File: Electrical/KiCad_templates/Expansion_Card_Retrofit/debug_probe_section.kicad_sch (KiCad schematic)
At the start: 15 parts, among them U3 W25Q16JVUXIQ, U4 RP2040

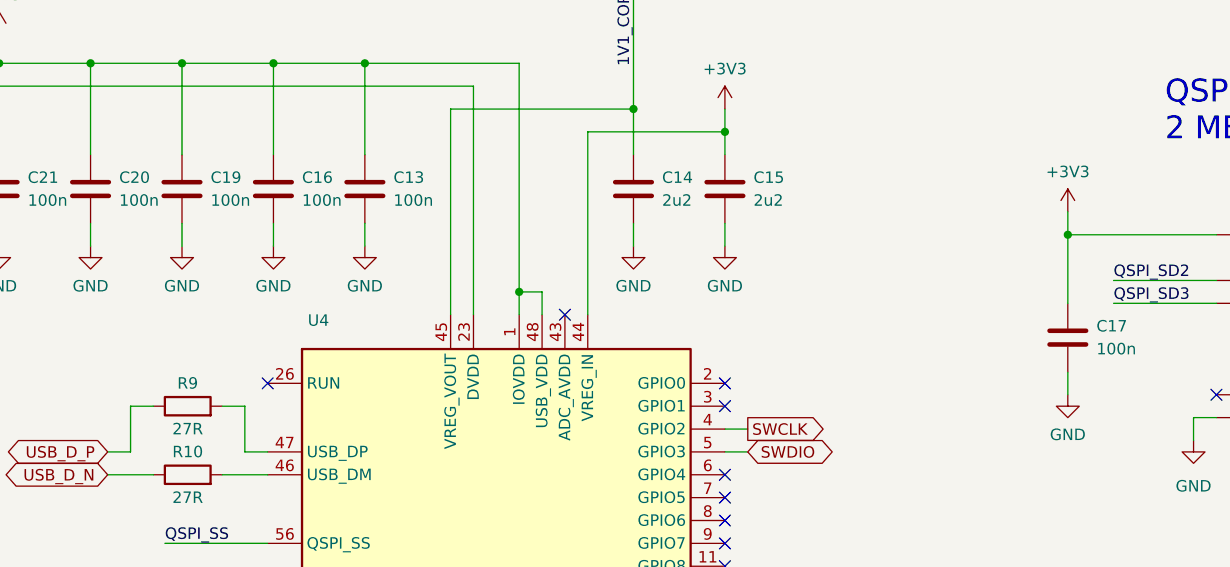
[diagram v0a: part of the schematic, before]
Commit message: Added test points
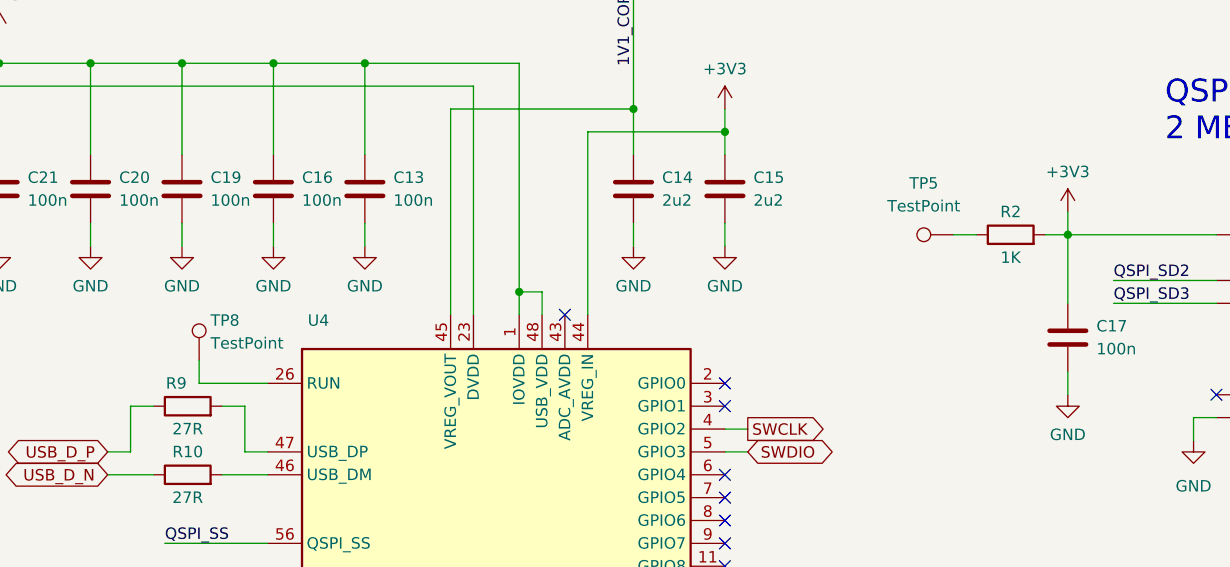
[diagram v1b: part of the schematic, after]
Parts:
- added R2: 1K, Resistor_SMD:R_0402_1005Metric, symbol Device:R
- added TP5, TP8: TestPoint, TestPoint:TestPoint_Pad_1.0x1.0mm, symbol Connector:TestPoint
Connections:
- net +3V3: now also R2.2
- net at U4.26 (RUN): now also TP8.1
- new net: R2.1, TP5.1
- no-connect marks 33 -> 32
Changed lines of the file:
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@@
   (no_connect (at 109.22 117.475))
   (no_connect (at 109.22 97.155))
-  (no_connect (at 58.42 74.295))
   (no_connect (at 109.22 142.875))
   (no_connect (at 109.22 135.255))
@@
     (stroke (width 0) (type default))
   )
+  (wire (pts (xy 144.78 57.785) (xy 147.32 57.785))
+    (stroke (width 0) (type default))
+  )
   (wire (pts (xy 147.32 57.785) (xy 163.83 57.785))
     (stroke (width 0) (type default))
@@
     (stroke (width 0) (type default))
   )
+  (wire (pts (xy 50.8 74.295) (xy 58.42 74.295))
+    (stroke (width 0) (type default))
+  )
   (wire (pts (xy 93.98 46.355) (xy 93.98 66.675))
     (stroke (width 0) (type default))
@@
     (stroke (width 0) (type default))
   )
+  (wire (pts (xy 50.8 71.755) (xy 50.8 74.295))
+    (stroke (width 0) (type default))
+  )
   (wire (pts (xy 18.415 27.305) (xy 18.415 41.275))
     (stroke (width 0) (type default))
@@
   )
   (wire (pts (xy 161.29 78.105) (xy 163.83 78.105))
+    (stroke (width 0) (type default))
+  )
+  (wire (pts (xy 134.62 57.785) (xy 137.16 57.785))
     (stroke (width 0) (type default))
   )
@@
     )
   )
+  (symbol (lib_id "Connector:TestPoint") (at 134.62 57.785 90) (unit 1)
+    (in_bom yes) (on_board yes) (dnp no) (fields_autoplaced)
+    (property "Reference" "TP5" (at 131.318 52.07 90)
+      (effects (font (size 1.27 1.27)))
+    )
+    (property "Value" "TestPoint" (at 131.318 54.61 90)
+      (effects (font (size 1.27 1.27)))
+    )
+    (property "Footprint" "TestPoint:TestPoint_Pad_1.0x1.0mm" (at 134.62 52.705 0)
+      (effects (font (size 1.27 1.27)) hide)
+    )
+    (property "Datasheet" "~" (at 134.62 52.705 0)
+      (effects (font (size 1.27 1.27)) hide)
+    )
+    (pin "1")
+    (instances
+      (project "Expansion_Card_Retrofit"
+        (path "/fd9cf59f-f670-406e-98d4-36112036cae5/ba09e9cc-93bf-4b37-819d-b7ee30f73540"
+          (reference "TP5") (unit 1)
+        )
+        (path "/fd9cf59f-f670-406e-98d4-36112036cae5/1926ef64-bcc8-4db2-9a20-46648adcb359"
+          (reference "TP6") (unit 1)
+        )
+      )
+    )
+  )
   (symbol (lib_id "Device:R") (at 175.895 120.65 90) (unit 1)
     (in_bom yes) (on_board yes) (dnp no)
@@
     )
   )
+  (symbol (lib_id "Connector:TestPoint") (at 50.8 71.755 0) (unit 1)
+    (in_bom yes) (on_board yes) (dnp no)
+    (property "Reference" "TP8" (at 52.07 67.31 0)
+      (effects (font (size 1.27 1.27)) (justify left))
+    )
+    (property "Value" "TestPoint" (at 52.07 69.85 0)
+      (effects (font (size 1.27 1.27)) (justify left))
+    )
+    (property "Footprint" "TestPoint:TestPoint_Pad_1.0x1.0mm" (at 55.88 71.755 0)
+      (effects (font (size 1.27 1.27)) hide)
+    )
+    (property "Datasheet" "~" (at 55.88 71.755 0)
+      (effects (font (size 1.27 1.27)) hide)
+    )
+    (pin "1")
+    (instances
+      (project "Expansion_Card_Retrofit"
+        (path "/fd9cf59f-f670-406e-98d4-36112036cae5/1926ef64-bcc8-4db2-9a20-46648adcb359"
+          (reference "TP8") (unit 1)
+        )
+      )
+    )
+  )
   (symbol (lib_id "power:GND") (at 99.06 59.055 0) (unit 1)
     (in_bom yes) (on_board yes) (dnp no) (fields_autoplaced)
@@
   (symbol (lib_id "Device:R") (at 49.53 76.835 90) (unit 1)
     (in_bom yes) (on_board yes) (dnp no)
-    (property "Reference" "R9" (at 49.53 74.295 90)
+    (property "Reference" "R9" (at 48.26 74.295 90)
       (effects (font (size 1.27 1.27)))
     )
@@
         )
       )
+    )
+  )
+  (symbol (lib_id "Device:R") (at 140.97 57.785 90) (unit 1)
+    (in_bom yes) (on_board yes) (dnp no)
+    (property "Reference" "R2" (at 140.97 55.245 90)
+      (effects (font (size 1.27 1.27)))
+    )
+    (property "Value" "1K" (at 140.97 60.325 90)
+      (effects (font (size 1.27 1.27)))
+    )
+    (property "Footprint" "Resistor_SMD:R_0402_1005Metric" (at 140.97 59.563 90)
+      (effects (font (size 1.27 1.27)) hide)
+    )
+    (property "Datasheet" "~" (at 140.97 57.785 0)
+      (effects (font (size 1.27 1.27)) hide)
+    )
+    (pin "1")
+    (pin "2")
+    (instances
+      (project "Expansion_Card_Retrofit"
+        (path "/fd9cf59f-f670-406e-98d4-36112036cae5/ba09e9cc-93bf-4b37-819d-b7ee30f73540"
+          (reference "R2") (unit 1)
+        )
+        (path "/fd9cf59f-f670-406e-98d4-36112036cae5/1926ef64-bcc8-4db2-9a20-46648adcb359"
+          (reference "R3") (unit 1)
+        )
+      )
